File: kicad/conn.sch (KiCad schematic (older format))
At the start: 2 parts, among them J1704 idc2x17, J1705 idc2x17

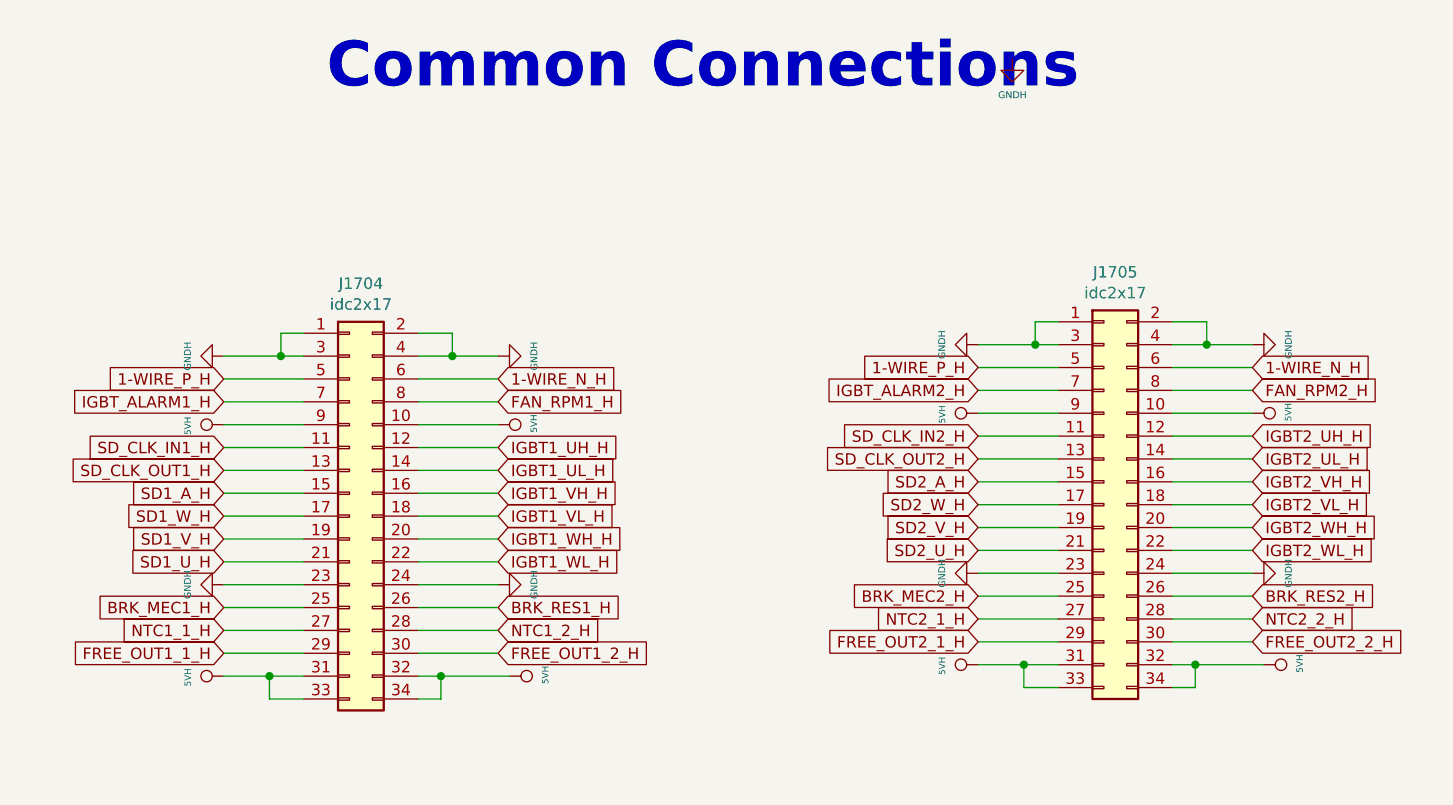
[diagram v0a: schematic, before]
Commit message: change in 5v interface scenario.. remove bridges
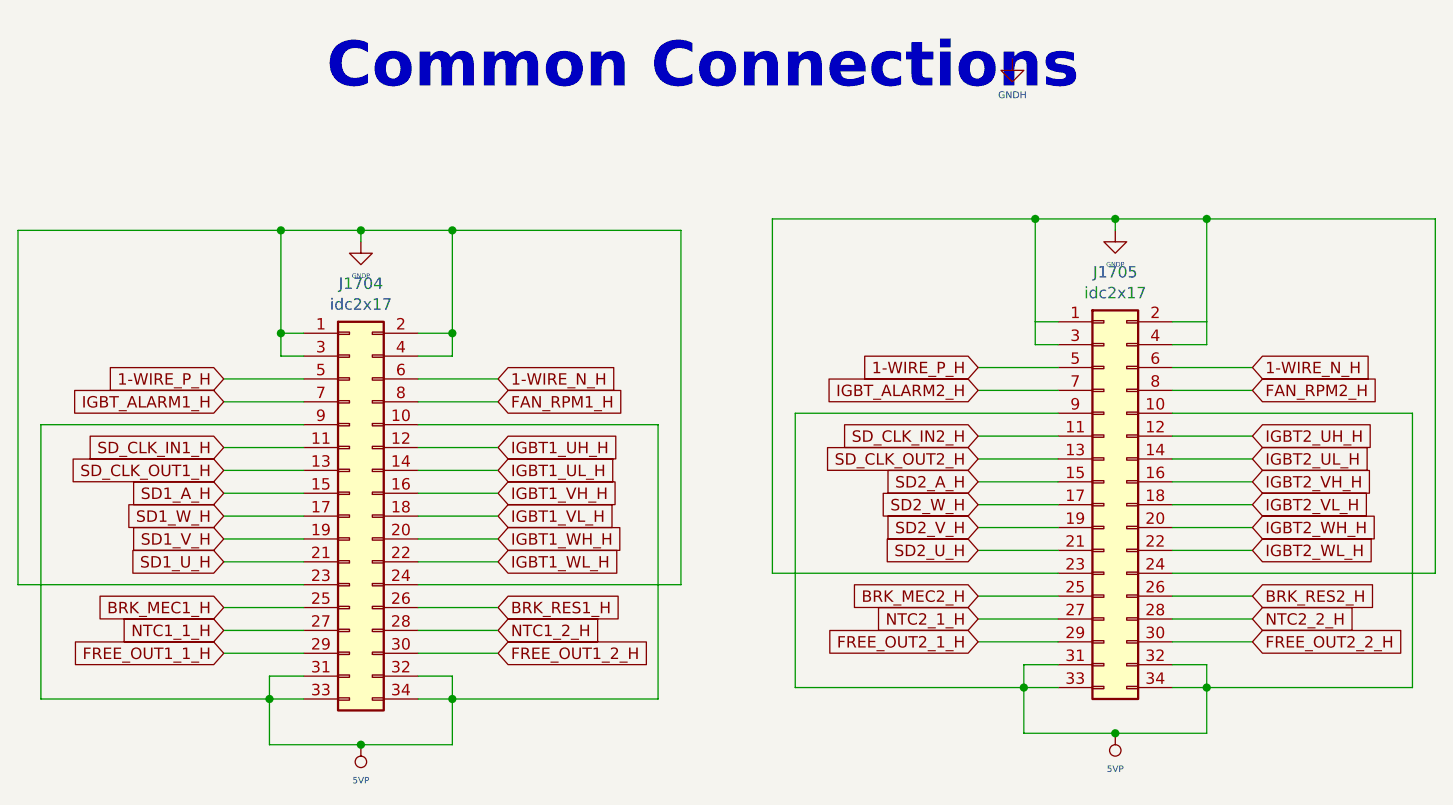
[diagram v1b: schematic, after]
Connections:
- net GNDH: no longer J1704.1 (Pin_1), J1704.2 (Pin_2), J1704.23 (Pin_23), J1704.24 (Pin_24), J1704.3 (Pin_3), J1704.4 (Pin_4), J1705.1 (Pin_1), J1705.2 (Pin_2), J1705.23 (Pin_23), J1705.24 (Pin_24), J1705.3 (Pin_3), J1705.4 (Pin_4)
- net 5VH renamed 5VP
- new net GNDP: J1704.1 (Pin_1), J1704.2 (Pin_2), J1704.23 (Pin_23), J1704.24 (Pin_24), J1704.3 (Pin_3), J1704.4 (Pin_4), J1705.1 (Pin_1), J1705.2 (Pin_2), J1705.23 (Pin_23), J1705.24 (Pin_24), J1705.3 (Pin_3), J1705.4 (Pin_4)

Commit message: more bom...
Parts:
- J1704, J1705: Description (none) -> Connector Header Surface Mount 34 position 0.100\" (2.54mm); PartNumber (none) -> SBH11-NBPC-D17-SM-BK; digikey (none) -> S9191-ND; price@10 (none) -> 1.31900
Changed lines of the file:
@@
 F 2 "servo:idc2x17_smd" H 6600 3050 50  0001 C CNN
 F 3 "~" H 6600 3050 50  0001 C CNN
+F 4 "Connector Header Surface Mount 34 position 0.100\" (2.54mm) " H 0   0   50  0001 C CNN "Description"
+F 5 "SBH11-NBPC-D17-SM-BK" H 0   0   50  0001 C CNN "PartNumber"
+F 6 "S9191-ND" H 0   0   50  0001 C CNN "digikey"
+F 7 "1.31900" H 0   0   50  0001 C CNN "price@10"
 	1    6600 3050
 	1    0    0    -1
@@
 F 2 "servo:idc2x17_smd" H 9900 3000 50  0001 C CNN
 F 3 "~" H 9900 3000 50  0001 C CNN
+F 4 "Connector Header Surface Mount 34 position 0.100\" (2.54mm) " H 0   0   50  0001 C CNN "Description"
+F 5 "SBH11-NBPC-D17-SM-BK" H 0   0   50  0001 C CNN "PartNumber"
+F 6 "S9191-ND" H 0   0   50  0001 C CNN "digikey"
+F 7 "1.31900" H 0   0   50  0001 C CNN "price@10"
 	1    9900 3000
 	1    0    0    -1

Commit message: gerbers + pnp + bom ready
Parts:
- J1704, J1705: bom_3 (none) -> 1
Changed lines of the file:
@@
 F 6 "S9191-ND" H 0   0   50  0001 C CNN "digikey"
 F 7 "1.31900" H 0   0   50  0001 C CNN "price@10"
+F 8 "" H 0   0   50  0001 C CNN "bom_1"
+F 9 "" H 0   0   50  0001 C CNN "bom_2"
+F 10 "1" H 0   0   50  0001 C CNN "bom_3"
 	1    6600 3050
 	1    0    0    -1
@@
 F 6 "S9191-ND" H 0   0   50  0001 C CNN "digikey"
 F 7 "1.31900" H 0   0   50  0001 C CNN "price@10"
+F 8 "" H 0   0   50  0001 C CNN "bom_1"
+F 9 "" H 0   0   50  0001 C CNN "bom_2"
+F 10 "1" H 0   0   50  0001 C CNN "bom_3"
 	1    9900 3000
 	1    0    0    -1

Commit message: some details on gerbers, now released
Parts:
- J1704, J1705: bom_1 (none) -> 0; bom_2 (none) -> 0
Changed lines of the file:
@@
 F 6 "S9191-ND" H 0   0   50  0001 C CNN "digikey"
 F 7 "1.31900" H 0   0   50  0001 C CNN "price@10"
-F 8 "" H 0   0   50  0001 C CNN "bom_1"
-F 9 "" H 0   0   50  0001 C CNN "bom_2"
+F 8 "0" H 0   0   50  0001 C CNN "bom_1"
+F 9 "0" H 0   0   50  0001 C CNN "bom_2"
 F 10 "1" H 0   0   50  0001 C CNN "bom_3"
 	1    6600 3050
@@
 F 6 "S9191-ND" H 0   0   50  0001 C CNN "digikey"
 F 7 "1.31900" H 0   0   50  0001 C CNN "price@10"
-F 8 "" H 0   0   50  0001 C CNN "bom_1"
-F 9 "" H 0   0   50  0001 C CNN "bom_2"
+F 8 "0" H 0   0   50  0001 C CNN "bom_1"
+F 9 "0" H 0   0   50  0001 C CNN "bom_2"
 F 10 "1" H 0   0   50  0001 C CNN "bom_3"
 	1    9900 3000
